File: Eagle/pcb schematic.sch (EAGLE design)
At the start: 21 parts

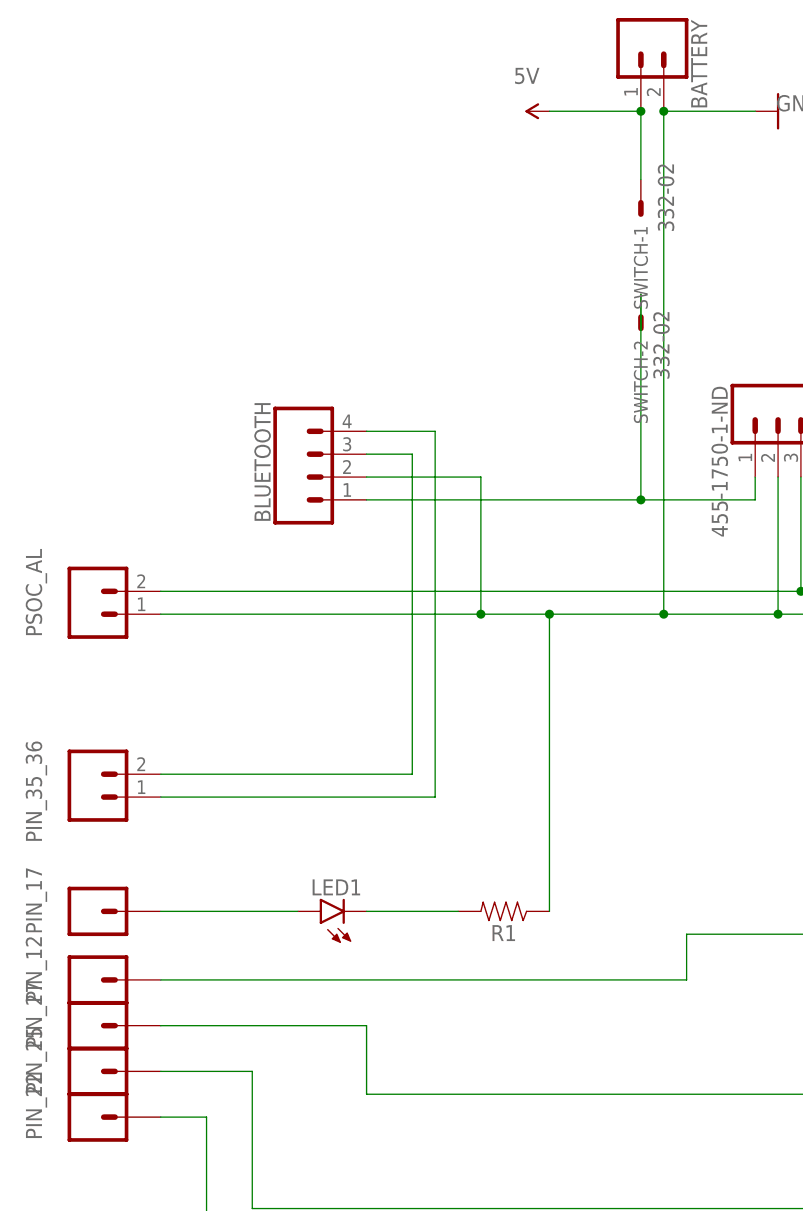
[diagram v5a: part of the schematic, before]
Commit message: PCB con aggiunta resistenze per carica batteria
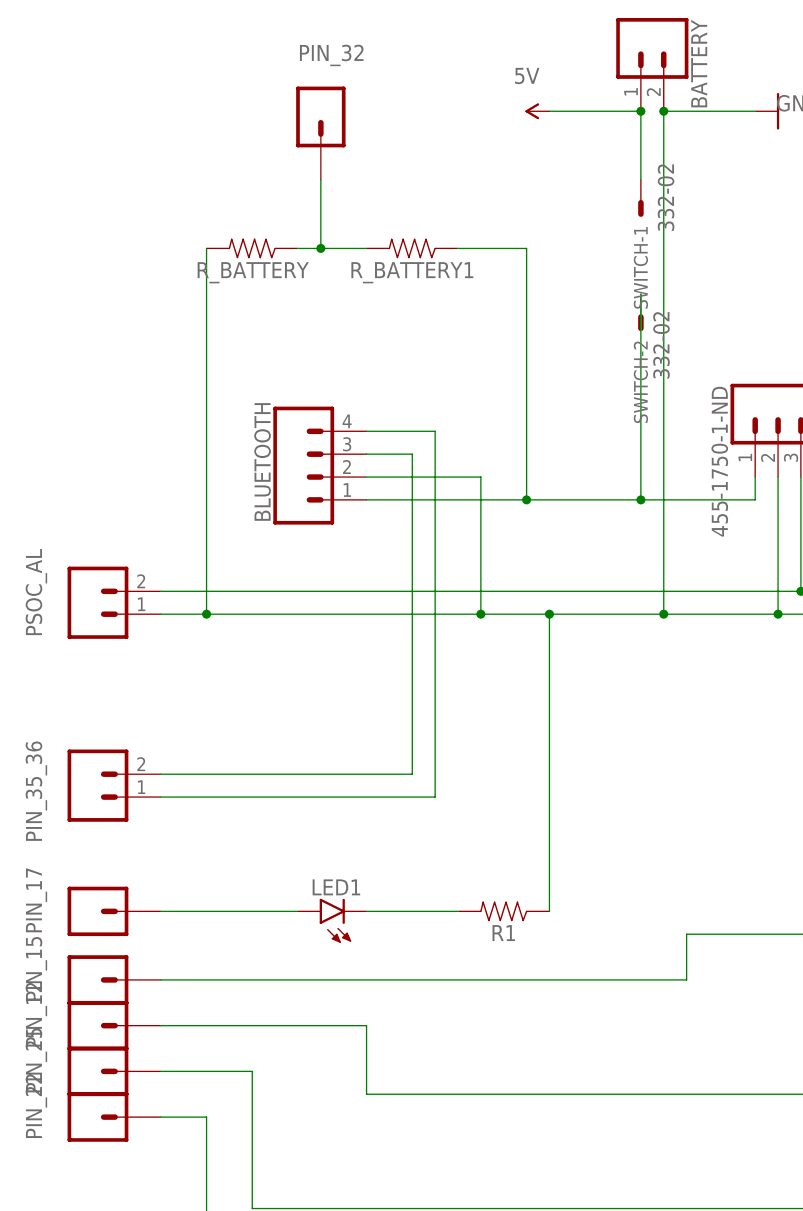
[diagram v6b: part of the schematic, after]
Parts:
- removed PIN_27: (no value), SparkFun-Connectors:CONN_01
- added PIN_15, PIN_32: (no value), SparkFun-Connectors:CONN_01
- added R_BATTERY, R_BATTERY1: (no value), SparkFun-Resistors:RESISTORAXIAL-0.3
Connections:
- new net N$9: PIN_32.1, R_BATTERY.1, R_BATTERY1.2
- net GND: now also R_BATTERY.2
- net N$1: now also PIN_15.1; no longer PIN_12.1
- net N$10: now also R_BATTERY1.1
- net N$2: now also PIN_12.1; no longer PIN_27.1
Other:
- moved on the sheet: PIN_12
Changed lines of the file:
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@@
 <part name="SWITCH" library="con-garry" library_urn="urn:adsk.eagle:library:147" deviceset="332-02" device="" package3d_urn="urn:adsk.eagle:package:6810/1"/>
 <part name="STABILIZZATORE" library="SparkFun-Connectors" deviceset="CONN_03" device="" value="455-1750-1-ND"/>
+<part name="PIN_15" library="SparkFun-Connectors" deviceset="CONN_01" device=""/>
 <part name="PIN_12" library="SparkFun-Connectors" deviceset="CONN_01" device=""/>
-<part name="PIN_27" library="SparkFun-Connectors" deviceset="CONN_01" device=""/>
 <part name="PIN_25" library="SparkFun-Connectors" deviceset="CONN_01" device=""/>
 <part name="PIN_22" library="SparkFun-Connectors" deviceset="CONN_01" device=""/>
+<part name="R_BATTERY" library="SparkFun-Resistors" deviceset="RESISTOR" device="AXIAL-0.3" value=" "/>
+<part name="R_BATTERY1" library="SparkFun-Resistors" deviceset="RESISTOR" device="AXIAL-0.3" value=" "/>
+<part name="PIN_32" library="SparkFun-Connectors" deviceset="CONN_01" device=""/>
 </parts>
 <sheets>
@@
 <attribute name="NAME" x="25.908" y="99.06" size="1.778" layer="95" font="vector" rot="R270"/>
 </instance>
-<instance part="PIN_12" gate="G$1" x="-55.88" y="33.02" smashed="yes">
+<instance part="PIN_15" gate="G$1" x="-55.88" y="33.02" smashed="yes">
 <attribute name="VALUE" x="-58.42" y="28.194" size="1.778" layer="96" font="vector"/>
 <attribute name="NAME" x="-61.468" y="30.48" size="1.778" layer="95" font="vector" rot="R90"/>
 </instance>
-<instance part="PIN_27" gate="G$1" x="-55.88" y="27.94" smashed="yes">
+<instance part="PIN_12" gate="G$1" x="-55.88" y="27.94" smashed="yes">
 <attribute name="VALUE" x="-58.42" y="23.114" size="1.778" layer="96" font="vector"/>
 <attribute name="NAME" x="-61.468" y="25.4" size="1.778" layer="95" font="vector" rot="R90"/>
@@
 <attribute name="VALUE" x="-58.42" y="12.954" size="1.778" layer="96" font="vector"/>
 <attribute name="NAME" x="-61.468" y="15.24" size="1.778" layer="95" font="vector" rot="R90"/>
+</instance>
+<instance part="R_BATTERY" gate="G$1" x="-38.1" y="114.3" smashed="yes" rot="R180">
+<attribute name="NAME" x="-38.1" y="112.776" size="1.778" layer="95" font="vector" rot="R180" align="bottom-center"/>
+<attribute name="VALUE" x="-38.1" y="115.824" size="1.778" layer="96" font="vector" rot="R180" align="top-center"/>
+</instance>
+<instance part="R_BATTERY1" gate="G$1" x="-20.32" y="114.3" smashed="yes" rot="R180">
+<attribute name="NAME" x="-20.32" y="112.776" size="1.778" layer="95" font="vector" rot="R180" align="bottom-center"/>
+<attribute name="VALUE" x="-20.32" y="115.824" size="1.778" layer="96" font="vector" rot="R180" align="top-center"/>
+</instance>
+<instance part="PIN_32" gate="G$1" x="-30.48" y="129.54" smashed="yes" rot="R270">
+<attribute name="VALUE" x="-35.306" y="132.08" size="1.778" layer="96" font="vector" rot="R270"/>
+<attribute name="NAME" x="-33.02" y="135.128" size="1.778" layer="95" font="vector"/>
 </instance>
 </instances>
@@
 <wire x1="43.18" y1="20.32" x2="-25.4" y2="20.32" width="0.1524" layer="91"/>
 <wire x1="-25.4" y1="20.32" x2="-25.4" y2="27.94" width="0.1524" layer="91"/>
-<pinref part="PIN_27" gate="G$1" pin="1"/>
+<pinref part="PIN_12" gate="G$1" pin="1"/>
 <wire x1="-25.4" y1="27.94" x2="-48.26" y2="27.94" width="0.1524" layer="91"/>
 </segment>
@@
 <pinref part="R5" gate="G$1" pin="1"/>
 <wire x1="27.94" y1="38.1" x2="27.94" y2="35.56" width="0.1524" layer="91"/>
-<pinref part="PIN_12" gate="G$1" pin="1"/>
+<pinref part="PIN_15" gate="G$1" pin="1"/>
 <wire x1="-48.26" y1="33.02" x2="10.16" y2="33.02" width="0.1524" layer="91"/>
 <wire x1="10.16" y1="33.02" x2="10.16" y2="38.1" width="0.1524" layer="91"/>
@@
 <wire x1="7.62" y1="73.66" x2="20.32" y2="73.66" width="0.1524" layer="91"/>
 <wire x1="20.32" y1="73.66" x2="27.94" y2="73.66" width="0.1524" layer="91"/>
-<wire x1="-48.26" y1="73.66" x2="-12.7" y2="73.66" width="0.1524" layer="91"/>
+<wire x1="-48.26" y1="73.66" x2="-43.18" y2="73.66" width="0.1524" layer="91"/>
 <pinref part="PSOC_AL" gate="G$1" pin="1"/>
+<wire x1="-43.18" y1="73.66" x2="-12.7" y2="73.66" width="0.1524" layer="91"/>
 <wire x1="7.62" y1="73.66" x2="-5.08" y2="73.66" width="0.1524" layer="91"/>
 <junction x="7.62" y="73.66"/>
@@
 <pinref part="R8" gate="G$1" pin="2"/>
 <wire x1="73.66" y1="17.78" x2="73.66" y2="73.66" width="0.1524" layer="91"/>
+<pinref part="R_BATTERY" gate="G$1" pin="2"/>
+<wire x1="-43.18" y1="114.3" x2="-43.18" y2="73.66" width="0.1524" layer="91"/>
+<junction x="-43.18" y="73.66"/>
 </segment>
 </net>
@@
 <wire x1="5.08" y1="109.22" x2="5.08" y2="86.36" width="0.1524" layer="91"/>
 <pinref part="BLUETOOTH" gate="G$1" pin="1"/>
-<wire x1="-25.4" y1="86.36" x2="5.08" y2="86.36" width="0.1524" layer="91"/>
+<wire x1="-25.4" y1="86.36" x2="-7.62" y2="86.36" width="0.1524" layer="91"/>
+<wire x1="-7.62" y1="86.36" x2="5.08" y2="86.36" width="0.1524" layer="91"/>
 <wire x1="5.08" y1="86.36" x2="17.78" y2="86.36" width="0.1524" layer="91"/>
 <junction x="5.08" y="86.36"/>
 <pinref part="STABILIZZATORE" gate="J$1" pin="1"/>
 <wire x1="17.78" y1="86.36" x2="17.78" y2="88.9" width="0.1524" layer="91"/>
+<wire x1="-7.62" y1="86.36" x2="-7.62" y2="114.3" width="0.1524" layer="91"/>
+<junction x="-7.62" y="86.36"/>
+<pinref part="R_BATTERY1" gate="G$1" pin="1"/>
+<wire x1="-7.62" y1="114.3" x2="-15.24" y2="114.3" width="0.1524" layer="91"/>
 </segment>
 </net>
@@
 </segment>
 </net>
+<net name="N$9" class="0">
+<segment>
+<pinref part="R_BATTERY" gate="G$1" pin="1"/>
+<pinref part="R_BATTERY1" gate="G$1" pin="2"/>
+<wire x1="-33.02" y1="114.3" x2="-30.48" y2="114.3" width="0.1524" layer="91"/>
+<pinref part="PIN_32" gate="G$1" pin="1"/>
+<wire x1="-30.48" y1="114.3" x2="-25.4" y2="114.3" width="0.1524" layer="91"/>
+<wire x1="-30.48" y1="121.92" x2="-30.48" y2="114.3" width="0.1524" layer="91"/>
+<junction x="-30.48" y="114.3"/>
+</segment>
+</net>
